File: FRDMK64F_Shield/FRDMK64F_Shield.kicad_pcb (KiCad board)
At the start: 2 copper layers, 18 parts, among them J1 CONN_02X08, J2 CONN_02X10, J3 CONN_02X08, J4 CONN_02X06

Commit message: Primera versión del PCB completo.
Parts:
- BATTERY1, HALL_0, HALL_1, HALL_2, HALL_3, HALL_4, HALL_5: footprint Pin_Headers:Pin_Header_Straight_1x03_Pitch1.00mm -> Pin_Headers:Pin_Header_Straight_1x03_Pitch2.54mm; moved to B.Cu
- BREAK1, ENABLED1, HORN1, POWER1: footprint Pin_Headers:Pin_Header_Straight_1x02_Pitch1.00mm -> Pin_Headers:Pin_Header_Straight_1x02_Pitch2.54mm; moved to B.Cu
- CINTA1: footprint Pin_Headers:Pin_Header_Straight_1x08_Pitch1.00mm -> Pin_Headers:Pin_Header_Straight_1x08_Pitch2.54mm; moved to B.Cu
- J1, J3: footprint Socket_Strips:Socket_Strip_Straight_2x08_Pitch2.00mm -> Socket_Strips:Socket_Strip_Straight_2x08_Pitch2.54mm; moved to B.Cu
- J2: footprint Socket_Strips:Socket_Strip_Straight_2x10_Pitch2.00mm -> Socket_Strips:Socket_Strip_Straight_2x10_Pitch2.54mm; moved to B.Cu
- J4: footprint Socket_Strips:Socket_Strip_Straight_2x06_Pitch2.00mm -> Socket_Strips:Socket_Strip_Straight_2x06_Pitch2.54mm; moved to B.Cu
- ULTRASONIC_1, ULTRASONIC_2: footprint Pin_Headers:Pin_Header_Straight_1x04_Pitch1.00mm -> Pin_Headers:Pin_Header_Straight_1x04_Pitch2.54mm; moved to B.Cu
- moved BATTERY1 112.1 mm to (59.7, 64.9)
- moved POWER1 105.7 mm to (62.3, 72.6)
- moved HORN1 89.5 mm to (79.6, 56.5)
- moved J4 76.4 mm to (81.9, 81.1), turned to 0 degrees
- moved J3 74.6 mm to (81.8, 103.9), turned to 0 degrees
- moved CINTA1 54.1 mm to (96.5, 55.1), turned to 0 degrees
- moved HALL_0 42.5 mm to (149.0, 119.7)
- moved ULTRASONIC_2 39.4 mm to (144.0, 132.5)
- moved HALL_1 38.6 mm to (149.0, 107.1)
- moved HALL_5 37.1 mm to (148.9, 56.4)
- moved HALL_2 36.0 mm to (149.0, 94.5)
- moved HALL_4 35.1 mm to (148.9, 69.1)
- moved HALL_3 34.7 mm to (148.9, 81.8)
- moved ULTRASONIC_1 32.0 mm to (143.8, 43.8)
- moved J1 22.2 mm to (124.9, 68.4), turned to 180 degrees
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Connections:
- J3 pad 14: /GND -> Net-(J3-Pad14)
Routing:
- net /GND: track 238.5 -> 381.2 mm, vias 0 -> 2
- net /P5V_USB: track 210.3 -> 325.3 mm
- net /REV_M3: track 23.9 -> 51.6 mm
- net /ULTRA1_ECHO: track 23.7 -> 49.6 mm
- net /REV_M2: track 25.0 -> 50.3 mm
- net /REV_M1: track 25.5 -> 50.4 mm
- net /REV_M0: track 25.9 -> 50.0 mm
- net /ULTRA1_TRIG: track 21.3 -> 42.4 mm
- net /ULTRA2_ECHO: track 27.6 -> 46.6 mm
- net /ULTRA2_TRIG: track 24.8 -> 41.9 mm
- net /HALL5_INT: track 23.1 -> 39.4 mm
- net /HORN: track 36.8 -> 22.6 mm
- net Net-(ENABLED1-Pad2): track 16.1 -> 29.9 mm
- net /BREAK: track 17.2 -> 29.2 mm
- net /I2C_SDA: track 90.0 -> 101.2 mm
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- added copper zone on F.Cu, net (none)
- added copper zone on F.Cu, net /GND
- removed copper zone on B.Cu, net /GND
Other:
- net class Default: clearance 0.2 -> 0.4; trace_width 0.25 -> 0.8
- rule trace_clearance: 0.2 -> 0.4

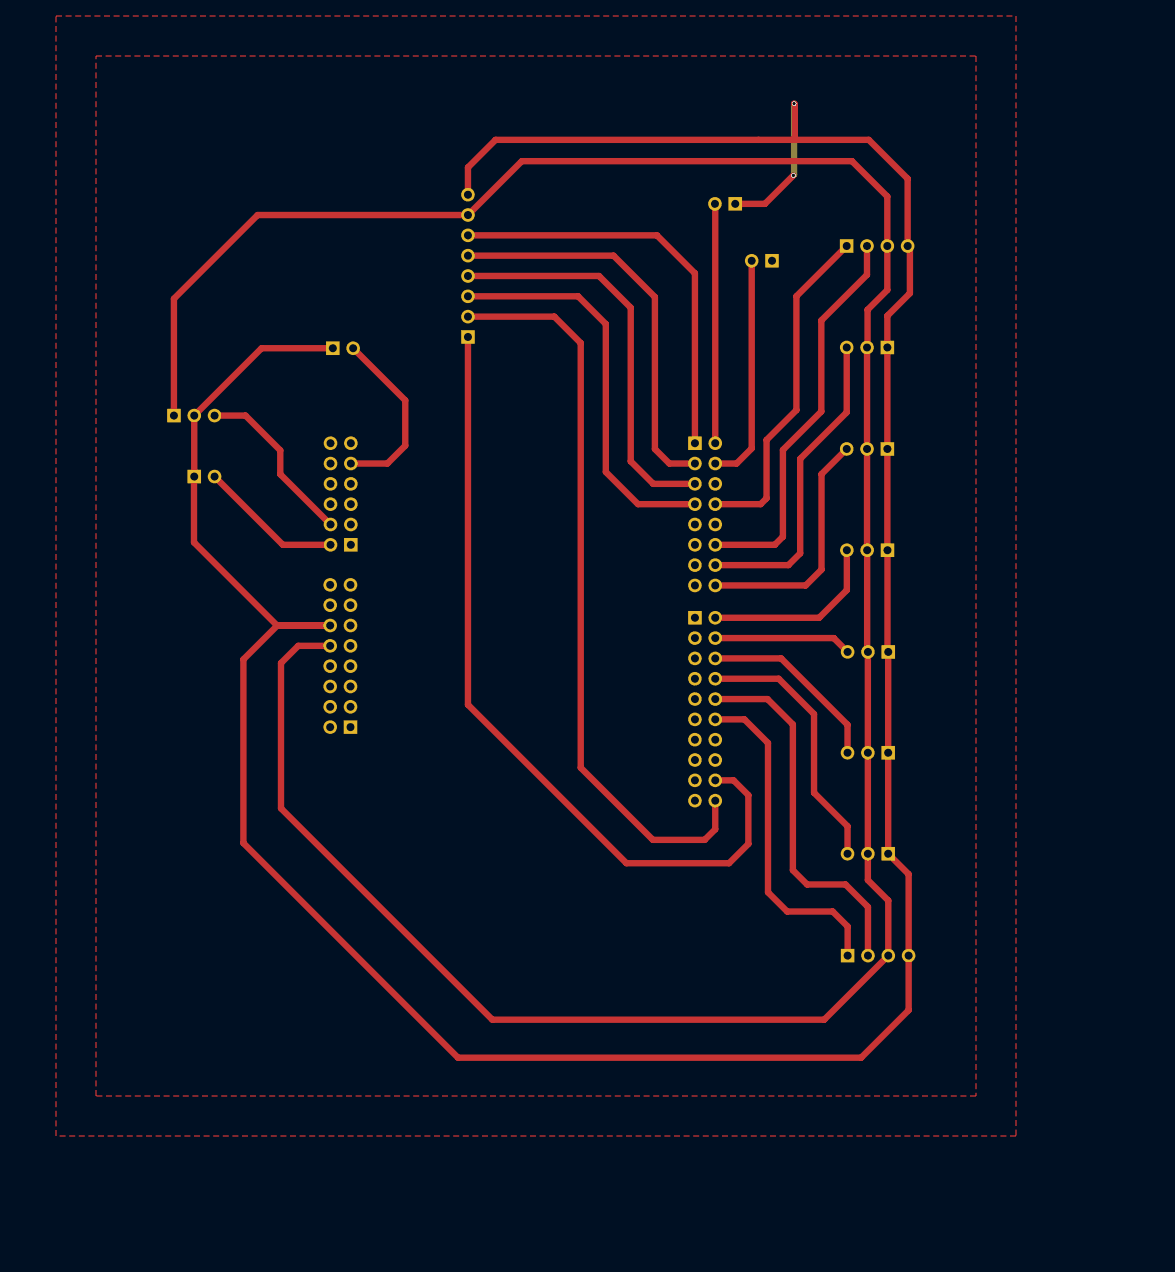
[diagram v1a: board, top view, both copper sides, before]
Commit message: Modificaciones en PCB.
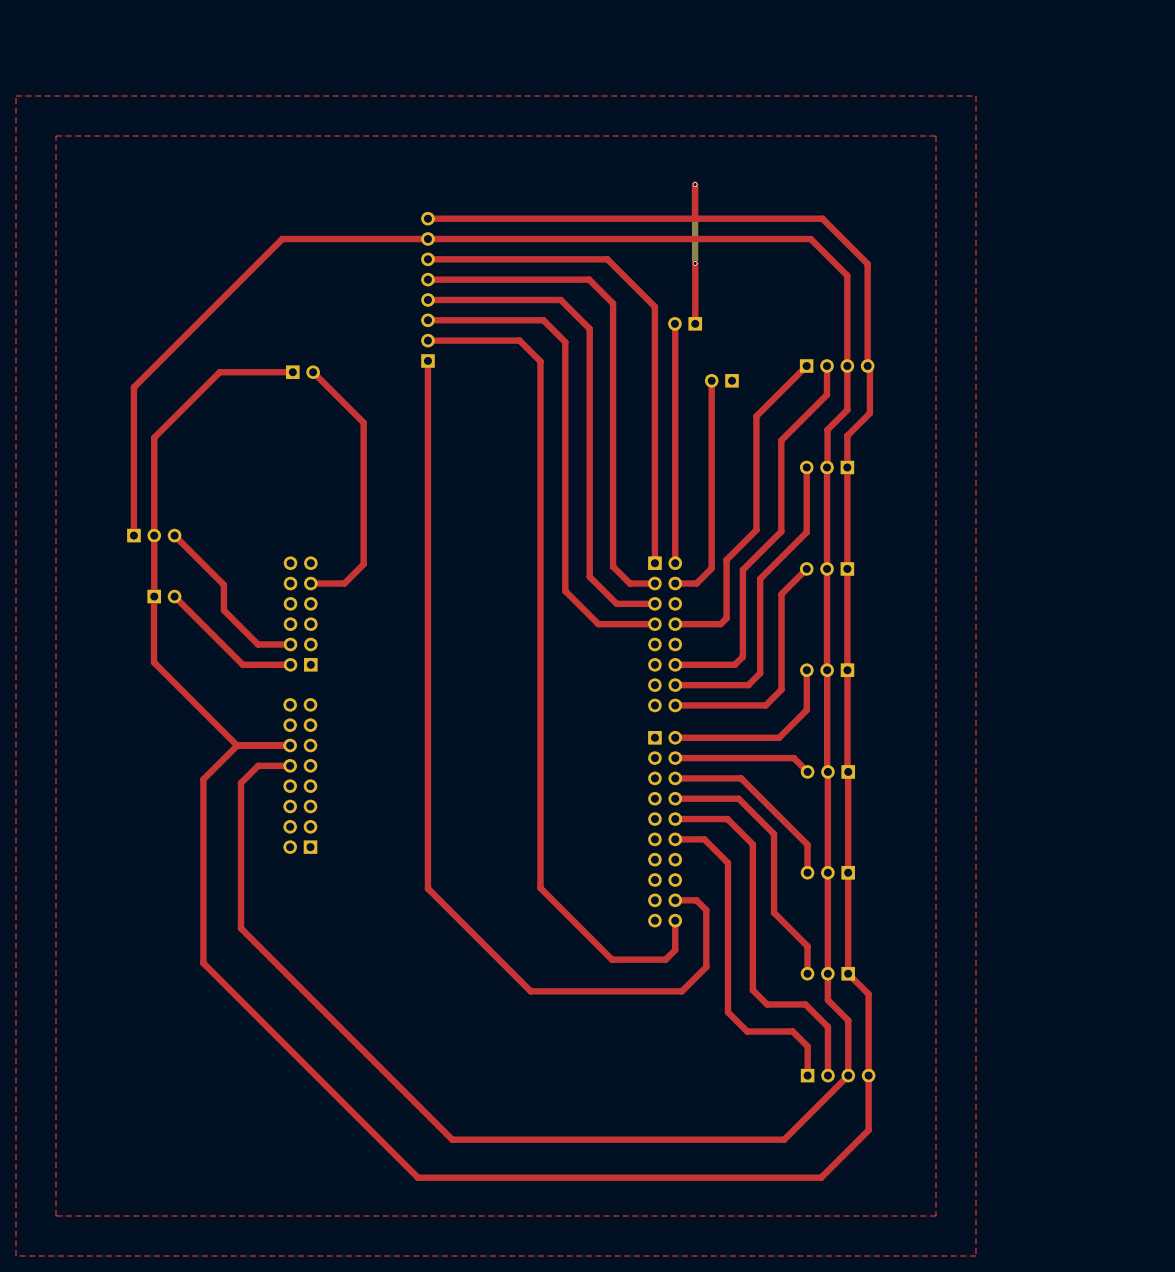
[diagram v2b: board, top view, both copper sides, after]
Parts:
- moved BATTERY1 15.8 mm to (54.7, 79.9)
- moved BREAK1 15.8 mm to (129.5, 60.6)
- moved ENABLED1 15.8 mm to (124.9, 53.5)
- moved HALL_0 15.8 mm to (144.0, 134.7)
- moved HALL_1 15.8 mm to (144.0, 122.1)
- moved HALL_2 15.8 mm to (144.0, 109.5)
- moved HALL_3 15.8 mm to (143.9, 96.8)
- moved HALL_4 15.8 mm to (143.9, 84.1)
- moved HALL_5 15.8 mm to (143.9, 71.4)
- moved J1 15.8 mm to (119.9, 83.4)
- moved J2 15.8 mm to (119.9, 105.2)
- moved J3 15.8 mm to (76.8, 118.9)
- moved J4 15.8 mm to (76.9, 96.1)
- moved POWER1 15.8 mm to (57.3, 87.6)
- moved ULTRASONIC_1 15.8 mm to (138.8, 58.8)
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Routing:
- net /I2C_SDA: track 101.2 -> 118.8 mm
- net /REV_M2: track 50.3 -> 63.4 mm
- net /I2C_SCL: track 93.2 -> 105.7 mm
- net /REV_M0: track 50.0 -> 62.3 mm
- net /REV_M1: track 50.4 -> 62.3 mm
- net /GND: track 381.2 -> 392.9 mm
- net /HORN: track 22.6 -> 34.2 mm
- net /REV_M3: track 51.6 -> 62.9 mm
- net /P5V_USB: track 325.3 -> 335.0 mm
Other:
- net class Default: clearance 0.4 -> 0.5
- rule trace_clearance: 0.4 -> 0.5

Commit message: pcb versión final
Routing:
- net /P5V_USB: track 335.0 -> 360.9 mm
- net /GND: track 392.9 -> 413.4 mm
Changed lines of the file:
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@@
     (links 44)
     (no_connects 0)
-    (area 56.1358 19.971839 155.28204 146.111802)
+    (area 40 25 160.000001 170.000001)
     (thickness 1.6)
     (drawings 0)
@@
     )
   )
+  (segment (start 74.2734 106.1892) (end 67.8008 106.1892) (width 0.8) (layer F.Cu) (net 1) (status 400000))
+  (segment (start 146.57704 155.68296) (end 146.57704 147.45084) (width 0.8) (layer F.Cu) (net 1) (status 800000))
+  (segment (start 140.462 161.798) (end 146.57704 155.68296) (width 0.8) (layer F.Cu) (net 1))
+  (segment (start 69.723 161.798) (end 140.462 161.798) (width 0.8) (layer F.Cu) (net 1))
+  (segment (start 56.769 148.844) (end 69.723 161.798) (width 0.8) (layer F.Cu) (net 1))
+  (segment (start 56.769 117.221) (end 56.769 148.844) (width 0.8) (layer F.Cu) (net 1))
+  (segment (start 67.8008 106.1892) (end 56.769 117.221) (width 0.8) (layer F.Cu) (net 1))
   (segment (start 124.9083 53.481) (end 124.9083 45.96006) (width 0.8) (layer F.Cu) (net 1))
   (segment (start 124.88544 36.07184) (end 124.88544 40.338) (width 0.8) (layer F.Cu) (net 1))
@@
   (segment (start 57.2808 87.5678) (end 57.2808 79.9478) (width 0.8) (layer F.Cu) (net 1))
   (segment (start 74.2734 106.1892) (end 67.63704 106.1892) (width 0.8) (layer F.Cu) (net 1))
+  (segment (start 67.63704 106.1892) (end 57.25032 95.80248) (width 0.8) (layer F.Cu) (net 1))
   (segment (start 57.25032 95.80248) (end 57.25032 87.59828) (width 0.8) (layer F.Cu) (net 1))
-  (segment (start 67.63704 106.1892) (end 57.25032 95.80248) (width 0.8) (layer F.Cu) (net 1))
   (segment (start 57.25032 87.59828) (end 57.2808 87.5678) (width 0.8) (layer F.Cu) (net 1))
-  (segment (start 74.2734 106.1892) (end 67.6662 106.1892) (width 0.8) (layer F.Cu) (net 1))
   (segment (start 143.9202 71.43548) (end 143.9202 67.4764) (width 0.8) (layer F.Cu) (net 1))
   (segment (start 146.7396 64.657) (end 146.7396 59.0352) (width 0.8) (layer F.Cu) (net 1))
@@
   (segment (start 146.57704 147.45084) (end 146.57704 137.27228) (width 0.8) (layer F.Cu) (net 1))
   (segment (start 146.57704 137.27228) (end 144.0218 134.71704) (width 0.8) (layer F.Cu) (net 1))
-  (segment (start 146.57704 154.27836) (end 146.57704 147.45084) (width 0.8) (layer F.Cu) (net 1))
-  (segment (start 140.6436 160.2118) (end 146.57704 154.27836) (width 0.8) (layer F.Cu) (net 1))
-  (segment (start 90.25 160.2118) (end 140.6436 160.2118) (width 0.8) (layer F.Cu) (net 1))
-  (segment (start 63.4276 133.3894) (end 90.25 160.2118) (width 0.8) (layer F.Cu) (net 1))
-  (segment (start 63.4276 110.4278) (end 63.4276 133.3894) (width 0.8) (layer F.Cu) (net 1))
-  (segment (start 67.6662 106.1892) (end 63.4276 110.4278) (width 0.8) (layer F.Cu) (net 1))
+  (segment (start 144.03704 147.45084) (end 144.03704 153.77796) (width 0.8) (layer F.Cu) (net 2) (status 400000))
+  (segment (start 60.452 122.5506) (end 74.2734 108.7292) (width 0.8) (layer F.Cu) (net 2) (status 800000))
+  (segment (start 60.452 147.574) (end 60.452 122.5506) (width 0.8) (layer F.Cu) (net 2))
+  (segment (start 71.755 158.877) (end 60.452 147.574) (width 0.8) (layer F.Cu) (net 2))
+  (segment (start 138.938 158.877) (end 71.755 158.877) (width 0.8) (layer F.Cu) (net 2))
+  (segment (start 144.03704 153.77796) (end 138.938 158.877) (width 0.8) (layer F.Cu) (net 2))
   (segment (start 91.4946 42.878) (end 73.294 42.878) (width 0.8) (layer F.Cu) (net 2))
   (segment (start 54.7408 61.4312) (end 54.7408 79.9478) (width 0.8) (layer F.Cu) (net 2))
@@
   (segment (start 141.4818 138.0122) (end 141.4818 134.71704) (width 0.8) (layer F.Cu) (net 2))
   (segment (start 144.03704 140.56744) (end 141.4818 138.0122) (width 0.8) (layer F.Cu) (net 2))
-  (segment (start 74.2734 108.7292) (end 70.2824 108.7292) (width 0.8) (layer F.Cu) (net 2))
-  (segment (start 136.02588 155.462) (end 144.03704 147.45084) (width 0.8) (layer F.Cu) (net 2))
-  (segment (start 94.5426 155.462) (end 136.02588 155.462) (width 0.8) (layer F.Cu) (net 2))
-  (segment (start 68.1266 129.046) (end 94.5426 155.462) (width 0.8) (layer F.Cu) (net 2))
-  (segment (start 68.1266 110.885) (end 68.1266 129.046) (width 0.8) (layer F.Cu) (net 2))
-  (segment (start 70.2824 108.7292) (end 68.1266 110.885) (width 0.8) (layer F.Cu) (net 2))
   (segment (start 141.4818 134.71704) (end 141.4818 122.09324) (width 0.8) (layer F.Cu) (net 2))
   (segment (start 141.4818 122.09324) (end 141.49196 122.08308) (width 0.8) (layer F.Cu) (net 2))
